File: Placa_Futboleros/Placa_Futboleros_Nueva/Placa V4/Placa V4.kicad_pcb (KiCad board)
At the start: 2 copper layers, 100 x 70 mm, 31 parts, among them J1 LiPo, J2 MI_Ad, J3 MI_At, J4 MD_Ad, J5 MD_At, J6 Pilas, U1 ESP32_30p, U2 DRV8833, U3 DRV8833, U5 INA219AxD

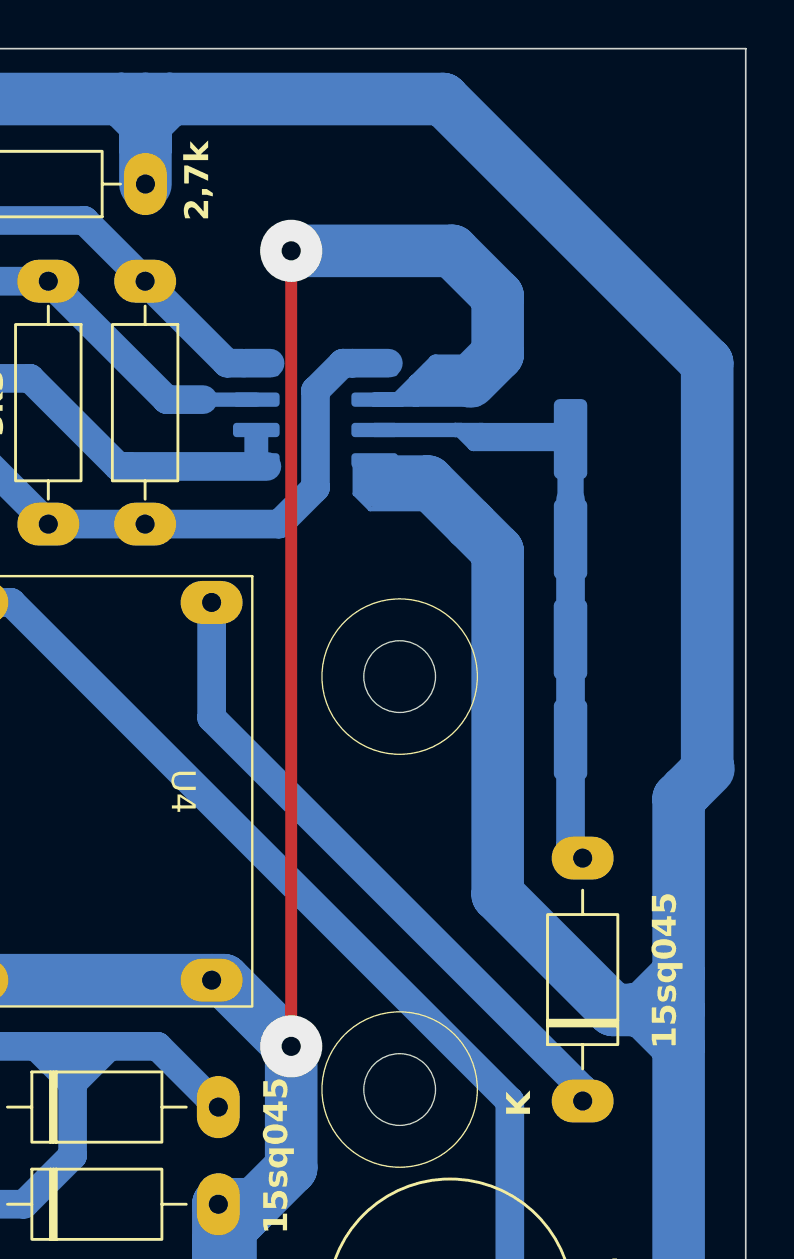
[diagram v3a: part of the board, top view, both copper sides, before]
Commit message: Pequeño cambio, se evita zona cercana al borde
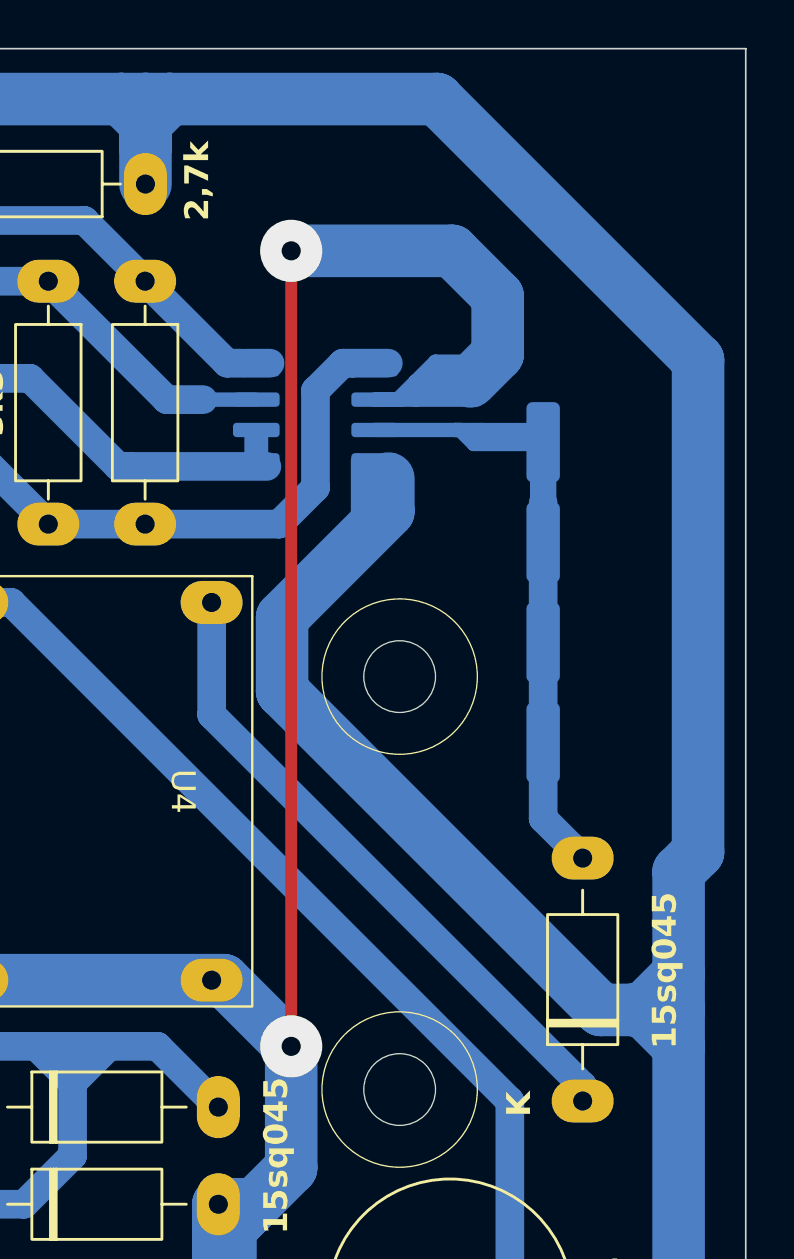
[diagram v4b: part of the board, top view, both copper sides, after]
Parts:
- moved R10 1.15 mm to (135.3, 56.1)
- moved R7 1.15 mm to (135.3, 43.5)
- moved R8 1.15 mm to (135.3, 47.7)
- moved R9 1.15 mm to (135.3, 51.9)
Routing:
- net VCC: track 315.7 -> 308.9 mm
- net Net-(D1-A): track 31.3 -> 30.7 mm
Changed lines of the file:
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@@
 	(footprint "Resistor_SMD:R_2512_6332Metric_Pad1.40x3.35mm_HandSolder"
 		(layer "B.Cu")
-		(at 136.435 55.955 180)
+		(at 135.29 56.082 180)
 		(descr "Resistor SMD 2512 (6332 Metric), square (rectangular) end terminal, IPC-7351 nominal with elongated pad for handsoldering. (Body size source: IPC-SM-782 page 72, https://www.pcb-3d.com/wordpress/wp-content/uploads/ipc-sm-782a_amendment_1_and_2.pdf)")
 		(tags "resistor handsolder")
@@
 	(footprint "Resistor_SMD:R_2512_6332Metric_Pad1.40x3.35mm_HandSolder"
 		(layer "B.Cu")
-		(at 136.435 47.573 180)
+		(at 135.29 47.7 180)
 		(descr "Resistor SMD 2512 (6332 Metric), square (rectangular) end terminal, IPC-7351 nominal with elongated pad for handsoldering. (Body size source: IPC-SM-782 page 72, https://www.pcb-3d.com/wordpress/wp-content/uploads/ipc-sm-782a_amendment_1_and_2.pdf)")
 		(tags "resistor handsolder")
@@
 	(footprint "Resistor_SMD:R_2512_6332Metric_Pad1.40x3.35mm_HandSolder"
 		(layer "B.Cu")
-		(at 136.433 51.764 180)
+		(at 135.288 51.891 180)
 		(descr "Resistor SMD 2512 (6332 Metric), square (rectangular) end terminal, IPC-7351 nominal with elongated pad for handsoldering. (Body size source: IPC-SM-782 page 72, https://www.pcb-3d.com/wordpress/wp-content/uploads/ipc-sm-782a_amendment_1_and_2.pdf)")
 		(tags "resistor handsolder")
@@
 	(footprint "Resistor_SMD:R_2512_6332Metric_Pad1.40x3.35mm_HandSolder"
 		(layer "B.Cu")
-		(at 136.435 43.382 180)
+		(at 135.29 43.509 180)
 		(descr "Resistor SMD 2512 (6332 Metric), square (rectangular) end terminal, IPC-7351 nominal with elongated pad for handsoldering. (Body size source: IPC-SM-782 page 72, https://www.pcb-3d.com/wordpress/wp-content/uploads/ipc-sm-782a_amendment_1_and_2.pdf)")
 		(tags "resistor handsolder")
@@
 	)
 	(segment
+		(start 125.765 46.39825)
+		(end 121.32 50.84325)
+		(width 2.2)
+		(layer "B.Cu")
+		(net "VCC")
+	)
+	(segment
 		(start 136.1905 87.3355)
 		(end 137.905 85.621)
@@
 	)
 	(segment
-		(start 128.051 29.158)
-		(end 139.1 40.207)
-		(width 2.2)
-		(layer "B.Cu")
-		(net "VCC")
-	)
-	(segment
 		(start 67.106967 29.158)
 		(end 114.589 29.158)
@@
 	)
 	(segment
-		(start 137.905 58.42)
-		(end 138.211 58.114)
-		(width 2.2)
-		(layer "B.Cu")
-		(net "VCC")
-	)
-	(segment
 		(start 115.605 29.158)
 		(end 116.621 29.158)
@@
 	)
 	(segment
-		(start 127.67 44.271)
-		(end 126.781 45.16)
-		(width 0.2)
-		(layer "B.Cu")
-		(net "VCC")
-	)
-	(segment
-		(start 127.797 44.398)
-		(end 129.194 45.795)
-		(width 0.2)
-		(layer "B.Cu")
-		(net "VCC")
-	)
-	(segment
 		(start 116.621 29.158)
 		(end 115.605 30.174)
@@
 	)
 	(segment
+		(start 121.32 50.84325)
+		(end 121.32 53.923)
+		(width 2.2)
+		(layer "B.Cu")
+		(net "VCC")
+	)
+	(segment
 		(start 115.605 30.174)
 		(end 115.605 31.19)
@@
 	)
 	(segment
-		(start 129.194 45.795)
-		(end 129.194 46.938)
-		(width 0.2)
-		(layer "B.Cu")
-		(net "VCC")
-	)
-	(segment
 		(start 135.3535 93.7375)
 		(end 136.1905 92.9005)
@@
 	)
 	(segment
-		(start 127.416 45.16)
-		(end 125.384 45.16)
+		(start 64.470989 37.332989)
+		(end 68.234 41.096)
 		(width 2.2)
 		(layer "B.Cu")
@@
 	)
 	(segment
-		(start 64.470989 37.332989)
-		(end 68.234 41.096)
+		(start 116.621 29.158)
+		(end 127.797 29.158)
 		(width 2.2)
 		(layer "B.Cu")
@@
 	)
 	(segment
-		(start 124.622 44.271)
-		(end 124.368 44.525)
-		(width 0.2)
+		(start 125.765 45.033)
+		(end 125.765 46.39825)
+		(width 2.2)
 		(layer "B.Cu")
 		(net "VCC")
@@
 	)
 	(segment
-		(start 139.1 40.207)
-		(end 139.1 56.844)
+		(start 137.905 67.258)
+		(end 135.925 67.258)
 		(width 2.2)
 		(layer "B.Cu")
@@
 	)
 	(segment
-		(start 129.067 46.303)
-		(end 129.3845 45.9855)
-		(width 0.2)
-		(layer "B.Cu")
-		(net "VCC")
-	)
-	(segment
-		(start 130.337 48.081)
-		(end 130.337 62.432)
+		(start 115.605 29.158)
+		(end 115.605 32.714)
 		(width 2.2)
 		(layer "B.Cu")
@@
 	)
 	(segment
-		(start 137.905 67.258)
-		(end 135.925 67.258)
-		(width 2.2)
+		(start 124.495 44.271)
+		(end 124.495 47.573)
+		(width 0.6)
 		(layer "B.Cu")
 		(net "VCC")
 	)
 	(segment
-		(start 124.368 44.525)
-		(end 124.368 45.668)
+		(start 125.192 44.271)
+		(end 124.622 44.271)
 		(width 0.2)
 		(layer "B.Cu")
@@
 	)
 	(segment
-		(start 115.605 29.158)
-		(end 115.605 32.714)
+		(start 127.797 29.158)
+		(end 138.719 40.08)
 		(width 2.2)
 		(layer "B.Cu")
@@
 	)
 	(segment
-		(start 125.192 44.271)
-		(end 124.622 44.271)
-		(width 0.2)
-		(layer "B.Cu")
-		(net "VCC")
-	)
-	(segment
 		(start 117.002 91.896)
 		(end 115.224 91.896)
@@
 	)
 	(segment
-		(start 129.194 46.938)
-		(end 127.416 45.16)
+		(start 137.905 85.621)
+		(end 137.905 68.782)
 		(width 2.2)
 		(layer "B.Cu")
@@
 	)
 	(segment
-		(start 137.905 85.621)
-		(end 137.905 68.782)
+		(start 138.719 40.08)
+		(end 138.719 60.654)
 		(width 2.2)
 		(layer "B.Cu")
@@
 	)
 	(segment
-		(start 126.781 45.16)
-		(end 125.384 45.16)
-		(width 0.2)
-		(layer "B.Cu")
-		(net "VCC")
-	)
-	(segment
 		(start 64.519022 83.641)
 		(end 64.385978 83.507956)
@@
 	)
 	(segment
-		(start 129.194 46.938)
-		(end 130.337 48.081)
+		(start 121.32 53.923)
+		(end 134.655 67.258)
 		(width 2.2)
 		(layer "B.Cu")
@@
 	)
 	(segment
-		(start 130.337 62.432)
-		(end 135.163 67.258)
-		(width 2.2)
-		(layer "B.Cu")
-		(net "VCC")
-	)
-	(segment
 		(start 128.075 95.451)
 		(end 120.557 95.451)
@@
 	)
 	(segment
-		(start 132.9 90.857)
-		(end 128.306 95.451)
+		(start 138.719 60.654)
+		(end 137.905 61.468)
 		(width 2.2)
 		(layer "B.Cu")
@@
 	)
 	(segment
-		(start 135.163 67.258)
-		(end 135.925 67.258)
+		(start 132.9 90.857)
+		(end 128.306 95.451)
 		(width 2.2)
 		(layer "B.Cu")
@@
 	)
 	(segment
-		(start 124.368 45.668)
-		(end 125.003 46.303)
-		(width 0.2)
-		(layer "B.Cu")
-		(net "VCC")
-	)
-	(segment
-		(start 137.905 65.734)
-		(end 137.905 58.42)
+		(start 137.905 61.468)
+		(end 137.905 65.734)
 		(width 2.2)
 		(layer "B.Cu")
@@
 	)
 	(segment
-		(start 138.211 58.114)
-		(end 139.152 57.173)
-		(width 2.2)
-		(layer "B.Cu")
-		(net "VCC")
-	)
-	(segment
 		(start 120.557 95.451)
 		(end 117.002 91.896)
@@
 	)
 	(segment
-		(start 116.621 29.158)
-		(end 128.051 29.158)
+		(start 134.655 67.258)
+		(end 135.925 67.258)
 		(width 2.2)
 		(layer "B.Cu")
@@
 	)
 	(segment
-		(start 125.003 46.303)
-		(end 129.067 46.303)
-		(width 0.2)
-		(layer "B.Cu")
-		(net "VCC")
-	)
-	(segment
 		(start 47.466011 42.172011)
 		(end 49.438 44.144)
@@
 	)
 	(segment
-		(start 133.893 70.56)
-		(end 133.893 71.068)
+		(start 118.373 50.214)
+		(end 118.373 54.913)
 		(width 1.2)
 		(layer "B.Cu")
@@
 	)
 	(segment
-		(start 118.373 55.04)
-		(end 133.893 70.56)
+		(start 118.373 54.913)
+		(end 133.893 70.433)
 		(width 1.2)
 		(layer "B.Cu")
@@
 	)
 	(segment
-		(start 118.373 50.214)
-		(end 118.373 55.04)
+		(start 133.893 70.433)
+		(end 133.893 71.068)
 		(width 1.2)
 		(layer "B.Cu")
@@
 	)
 	(segment
-		(start 133.385 60.4)
-		(end 133.385 55.59)
-		(width 1.2)
-		(layer "B.Cu")
-		(net "Net-(D1-A)")
-	)
-	(segment
 		(start 128.559 43.001)
 		(end 128.813 43.001)
@@
 	)
 	(segment
-		(start 133.385 43.382)
-		(end 133.385 45.922)
+		(start 132.24 43.509)
+		(end 132.24 46.049)
 		(width 1.1)
 		(layer "B.Cu")
@@
 	)
 	(segment
-		(start 128.7495 43.0645)
-		(end 129.321 43.636)
-		(width 0.5)
+		(start 132.24 59.255)
+		(end 132.24 46.049)
+		(width 1.2)
 		(layer "B.Cu")
 		(net "Net-(D1-A)")
 	)
 	(segment
-		(start 133.131 43.636)
-		(end 133.385 43.382)
+		(start 131.986 43.763)
+		(end 132.24 43.509)
 		(width 0.5)
 		(layer "B.Cu")
@@
 	)
 	(segment
-		(start 129.575 43.255)
-		(end 133.258 43.255)
-		(width 1.1)
+		(start 133.893 60.908)
+		(end 132.24 59.255)
+		(width 1.2)
 		(layer "B.Cu")
 		(net "Net-(D1-A)")
@@
 	)
 	(segment
-		(start 133.385 45.922)
-		(end 133.385 48.97)
-		(width 1.2)
+		(start 131.986 43.255)
+		(end 132.24 43.509)
+		(width 1.1)
 		(layer "B.Cu")
 		(net "Net-(D1-A)")
 	)
 	(segment
-		(start 133.385 48.97)
-		(end 133.385 52.28)
-		(width 1.2)
+		(start 132.113 43.382)
+		(end 132.24 43.509)
+		(width 1.1)
 		(layer "B.Cu")
 		(net "Net-(D1-A)")
 	)
 	(segment
-		(start 133.258 43.255)
-		(end 133.385 43.382)
-		(width 1.1)
+		(start 132.113 43.636)
+		(end 132.24 43.509)
+		(width 0.5)
 		(layer "B.Cu")
 		(net "Net-(D1-A)")
 	)
 	(segment
-		(start 133.385 52.28)
-		(end 133.385 55.59)
-		(width 1.2)
+		(start 129.575 43.255)
+		(end 131.986 43.255)
+		(width 1.1)
 		(layer "B.Cu")
 		(net "Net-(D1-A)")
@@
 	(segment
 		(start 129.321 43.636)
-		(end 133.131 43.636)
+		(end 132.113 43.636)
+		(width 0.5)
+		(layer "B.Cu")
+		(net "Net-(D1-A)")
+	)
+	(segment
+		(start 128.7495 43.0645)
+		(end 129.321 43.636)
 		(width 0.5)
 		(layer "B.Cu")
